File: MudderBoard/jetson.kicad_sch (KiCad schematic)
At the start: 16 parts, among them Q6 CSD16327Q3, U9 LM3488QMM/NOPB

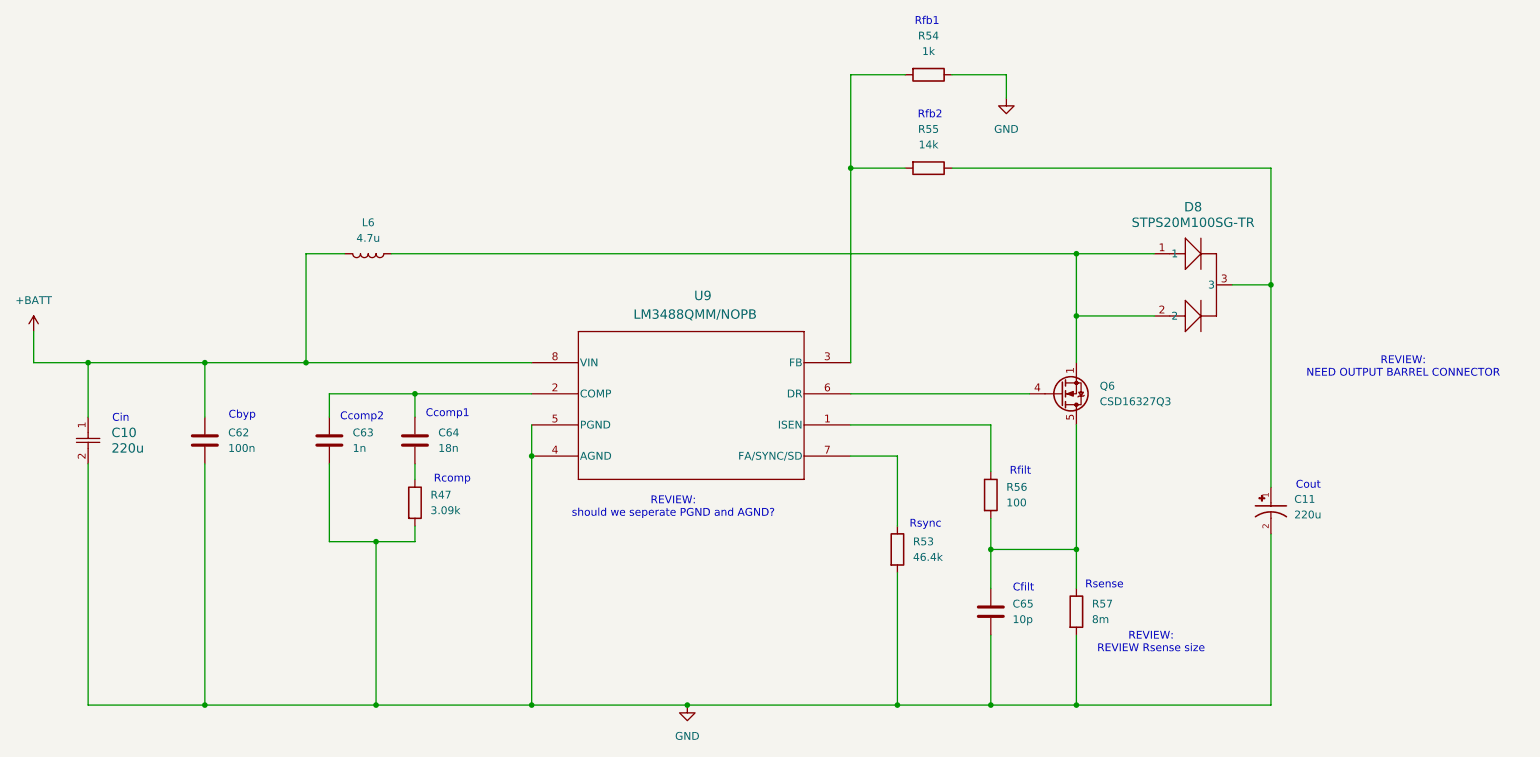
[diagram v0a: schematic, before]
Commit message: Imported footprints to layout
Colin - Make note of these

C30,C32 are generic 0805 caps
L4,L5 are basic insuctors, will need to change when we figure this situation out!

U8,U9 changed to same boost IC as Lidar - these are the same right?
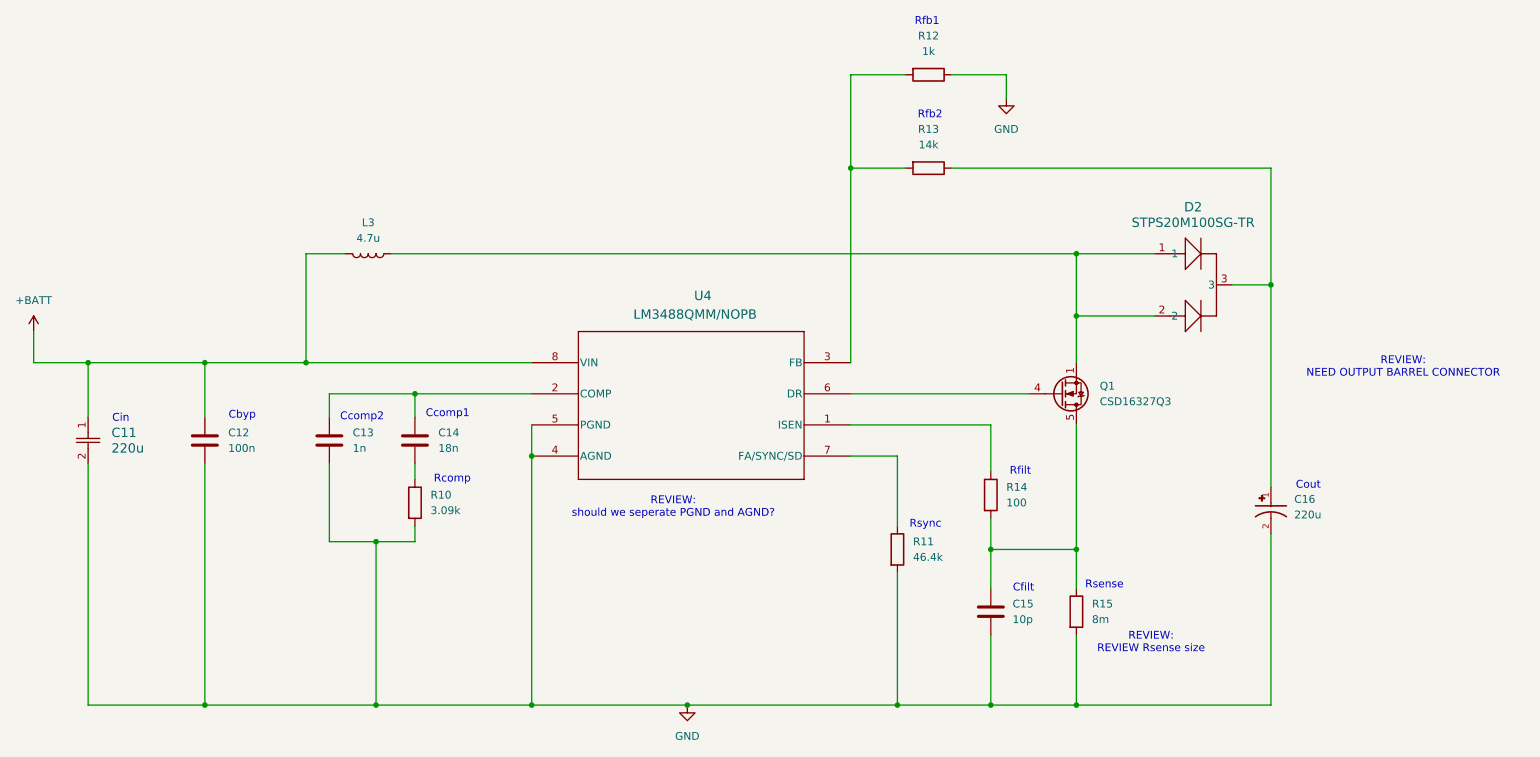
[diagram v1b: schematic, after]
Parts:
- renumbered C10 to C11, C62 to C12, C63 to C13, C64 to C14, C65 to C15, C11 to C16, D8 to D2, L6 to L3, Q6 to Q1, R47 to R10, R53 to R11, R54 to R12, R55 to R13, R56 to R14, R57 to R15, U9 to U4
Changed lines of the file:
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@@
 		(dnp no)
 		(fields_autoplaced yes)
-		(property "Reference" "R56"
+		(property "Reference" "R14"
 			(at 200.66 92.7099 0)
 			(effects
@@
 			(project "MudderBoard"
 				(path "/cdf98bf7-80ce-4b13-b655-e6c7c589c122/674dd553-7765-4ece-a996-68b5361f64e2"
-					(reference "R56")
+					(reference "R14")
 					(unit 1)
 				)
@@
 		(dnp no)
 		(fields_autoplaced yes)
-		(property "Reference" "C62"
+		(property "Reference" "C12"
 			(at 73.66 83.8199 0)
 			(effects
@@
 			(project "MudderBoard"
 				(path "/cdf98bf7-80ce-4b13-b655-e6c7c589c122/674dd553-7765-4ece-a996-68b5361f64e2"
-					(reference "C62")
+					(reference "C12")
 					(unit 1)
 				)
@@
 		(dnp no)
 		(fields_autoplaced yes)
-		(property "Reference" "R57"
+		(property "Reference" "R15"
 			(at 214.63 111.7599 0)
 			(effects
@@
 			(project "MudderBoard"
 				(path "/cdf98bf7-80ce-4b13-b655-e6c7c589c122/674dd553-7765-4ece-a996-68b5361f64e2"
-					(reference "R57")
+					(reference "R15")
 					(unit 1)
 				)
@@
 		(on_board yes)
 		(dnp no)
-		(property "Reference" "C65"
+		(property "Reference" "C15"
 			(at 201.676 111.76 0)
 			(effects
@@
 			(project "MudderBoard"
 				(path "/cdf98bf7-80ce-4b13-b655-e6c7c589c122/674dd553-7765-4ece-a996-68b5361f64e2"
-					(reference "C65")
+					(reference "C15")
 					(unit 1)
 				)
@@
 		(dnp no)
 		(fields_autoplaced yes)
-		(property "Reference" "#PWR016"
+		(property "Reference" "#PWR012"
 			(at 148.59 134.62 0)
 			(effects
@@
 			(project "MudderBoard"
 				(path "/cdf98bf7-80ce-4b13-b655-e6c7c589c122/674dd553-7765-4ece-a996-68b5361f64e2"
-					(reference "#PWR016")
+					(reference "#PWR012")
 					(unit 1)
 				)
@@
 		(dnp no)
 		(fields_autoplaced yes)
-		(property "Reference" "R47"
+		(property "Reference" "R10"
 			(at 106.68 93.9799 0)
 			(effects
@@
 			(project "MudderBoard"
 				(path "/cdf98bf7-80ce-4b13-b655-e6c7c589c122/674dd553-7765-4ece-a996-68b5361f64e2"
-					(reference "R47")
+					(reference "R10")
 					(unit 1)
 				)
@@
 		(dnp no)
 		(fields_autoplaced yes)
-		(property "Reference" "C11"
+		(property "Reference" "C16"
 			(at 247.65 94.6765 90)
 			(effects
@@
 			(project "MudderBoard"
 				(path "/cdf98bf7-80ce-4b13-b655-e6c7c589c122/674dd553-7765-4ece-a996-68b5361f64e2"
-					(reference "C11")
+					(reference "C16")
 					(unit 1)
 				)
@@
 		(dnp no)
 		(fields_autoplaced yes)
-		(property "Reference" "#PWR017"
+		(property "Reference" "#PWR013"
 			(at 200.66 35.56 0)
 			(effects
@@
 			(project "MudderBoard"
 				(path "/cdf98bf7-80ce-4b13-b655-e6c7c589c122/674dd553-7765-4ece-a996-68b5361f64e2"
-					(reference "#PWR017")
+					(reference "#PWR013")
 					(unit 1)
 				)
@@
 		(on_board yes)
 		(dnp no)
-		(property "Reference" "U9"
+		(property "Reference" "U4"
 			(at 151.13 61.468 0)
 			(effects
@@
 			(project "MudderBoard"
 				(path "/cdf98bf7-80ce-4b13-b655-e6c7c589c122/674dd553-7765-4ece-a996-68b5361f64e2"
-					(reference "U9")
+					(reference "U4")
 					(unit 1)
 				)
@@
 		(dnp no)
 		(fields_autoplaced yes)
-		(property "Reference" "C63"
+		(property "Reference" "C13"
 			(at 93.98 83.8199 0)
 			(effects
@@
 			(project "MudderBoard"
 				(path "/cdf98bf7-80ce-4b13-b655-e6c7c589c122/674dd553-7765-4ece-a996-68b5361f64e2"
-					(reference "C63")
+					(reference "C13")
 					(unit 1)
 				)
@@
 		(dnp no)
 		(fields_autoplaced yes)
-		(property "Reference" "R54"
+		(property "Reference" "R12"
 			(at 187.96 19.05 90)
 			(effects
@@
 			(project "MudderBoard"
 				(path "/cdf98bf7-80ce-4b13-b655-e6c7c589c122/674dd553-7765-4ece-a996-68b5361f64e2"
-					(reference "R54")
+					(reference "R12")
 					(unit 1)
 				)
@@
 		(dnp no)
 		(fields_autoplaced yes)
-		(property "Reference" "#PWR013"
+		(property "Reference" "#PWR011"
 			(at 41.91 71.12 0)
 			(effects
@@
 			(project "MudderBoard"
 				(path "/cdf98bf7-80ce-4b13-b655-e6c7c589c122/674dd553-7765-4ece-a996-68b5361f64e2"
-					(reference "#PWR013")
+					(reference "#PWR011")
 					(unit 1)
 				)
@@
 		(dnp no)
 		(fields_autoplaced yes)
-		(property "Reference" "R55"
+		(property "Reference" "R13"
 			(at 187.96 34.29 90)
 			(effects
@@
 			(project "MudderBoard"
 				(path "/cdf98bf7-80ce-4b13-b655-e6c7c589c122/674dd553-7765-4ece-a996-68b5361f64e2"
-					(reference "R55")
+					(reference "R13")
 					(unit 1)
 				)
@@
 		(on_board yes)
 		(dnp no)
-		(property "Reference" "Q6"
+		(property "Reference" "Q1"
 			(at 215.9 76.1999 0)
 			(effects
@@
 			(project "MudderBoard"
 				(path "/cdf98bf7-80ce-4b13-b655-e6c7c589c122/674dd553-7765-4ece-a996-68b5361f64e2"
-					(reference "Q6")
+					(reference "Q1")
 					(unit 1)
 				)
@@
 		(dnp no)
 		(fields_autoplaced yes)
-		(property "Reference" "C64"
+		(property "Reference" "C14"
 			(at 107.95 83.8199 0)
 			(effects
@@
 			(project "MudderBoard"
 				(path "/cdf98bf7-80ce-4b13-b655-e6c7c589c122/674dd553-7765-4ece-a996-68b5361f64e2"
-					(reference "C64")
+					(reference "C14")
 					(unit 1)
 				)
@@
 		(dnp no)
 		(fields_autoplaced yes)
-		(property "Reference" "C10"
+		(property "Reference" "C11"
 			(at 54.61 83.8199 90)
 			(effects
@@
 			(project "MudderBoard"
 				(path "/cdf98bf7-80ce-4b13-b655-e6c7c589c122/674dd553-7765-4ece-a996-68b5361f64e2"
-					(reference "C10")
+					(reference "C11")
 					(unit 1)
 				)
@@
 		(dnp no)
 		(fields_autoplaced yes)
-		(property "Reference" "D8"
+		(property "Reference" "D2"
 			(at 231.14 46.99 0)
 			(effects
@@
 			(project "MudderBoard"
 				(path "/cdf98bf7-80ce-4b13-b655-e6c7c589c122/674dd553-7765-4ece-a996-68b5361f64e2"
-					(reference "D8")
+					(reference "D2")
 					(unit 1)
 				)
@@
 		(dnp no)
 		(fields_autoplaced yes)
-		(property "Reference" "L6"
+		(property "Reference" "L3"
 			(at 96.52 49.53 90)
 			(effects
@@
 			(project "MudderBoard"
 				(path "/cdf98bf7-80ce-4b13-b655-e6c7c589c122/674dd553-7765-4ece-a996-68b5361f64e2"
-					(reference "L6")
+					(reference "L3")
 					(unit 1)
 				)
@@
 		(dnp no)
 		(fields_autoplaced yes)
-		(property "Reference" "R53"
+		(property "Reference" "R11"
 			(at 185.42 101.5999 0)
 			(effects
@@
 			(project "MudderBoard"
 				(path "/cdf98bf7-80ce-4b13-b655-e6c7c589c122/674dd553-7765-4ece-a996-68b5361f64e2"
-					(reference "R53")
-					(unit 1)
-				)
+					(reference "R11")
+					(unit 1)
+				)

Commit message: Schematic updates
global labels and test points
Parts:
- added TP42, TP43, TP44: TestPoint, TestPoint:TestPoint_Pad_1.0x1.0mm, symbol Connector:TestPoint
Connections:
- net +BATT: now also TP42.1
- net Vo?: now reaches C16.1, D2.3, R13.1
- net Vo?: now also TP44.1
- net at R12.2, R13.2, U4.3 (FB): now also TP43.1
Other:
- note added: "replace Vo with voltage level"

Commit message: Schematic and Layout
TPs and net labels
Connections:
- net Vo? renamed +19V
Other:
- note removed: "replace Vo with voltage level"
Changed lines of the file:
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@@
-		)
-	)
-	(text "replace Vo with voltage level\n"
-		(exclude_from_sim no)
-		(at 268.224 55.626 0)
-		(effects
-			(font
-				(size 1.27 1.27)
-			)
 		)
 	)
@@
 		)
 	)
-	(global_label "Vo?"
+	(global_label "+19V"
 		(shape input)
 		(at 259.08 59.69 0)
@@
 		)
 		(property "Intersheetrefs" "${INTERSHEET_REFS}"
-			(at 265.3914 59.69 0)
+			(at 267.1452 59.69 0)
 			(effects
 				(font
